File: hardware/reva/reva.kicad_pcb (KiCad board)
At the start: 2 copper layers, 65 x 28 mm, 9 parts, among them U1 ATSAMD21E17D-A, U2 DRV8833PWP, U3 MIC5504-3.3YM5, Y1 Crystal

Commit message: pcb placement
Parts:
- added C1: 10u 16V, Capacitor_SMD:C_0603_1608Metric, F.Cu at (132.0, 96.5)
- added C10: 10u 10V, Capacitor_SMD:C_0603_1608Metric, F.Cu at (149.2, 97.0)
- added C11: 100n, Capacitor_SMD:C_0603_1608Metric, F.Cu at (144.2, 102.0)
- added C12: 10n, Capacitor_SMD:C_0603_1608Metric, F.Cu at (161.0, 87.5)
- added C13: 2u2, Capacitor_SMD:C_0603_1608Metric, F.Cu at (161.0, 84.5)
- added C2: 1n, Capacitor_SMD:C_0603_1608Metric, F.Cu at (130.7, 89.0)
- added C3: 1n, Capacitor_SMD:C_0603_1608Metric, F.Cu at (130.5, 91.0)
- added C4: 10u 10V, Capacitor_SMD:C_0603_1608Metric, F.Cu at (135.0, 98.4)
- added C5: C, Capacitor_SMD:C_0603_1608Metric, F.Cu at (135.0, 101.8)
- added C6: C, Capacitor_SMD:C_0603_1608Metric, F.Cu at (142.0, 102.0)
- added C7: 10n, Capacitor_SMD:C_0603_1608Metric, F.Cu at (177.5, 101.5)
- added C8: 1u 25V, Capacitor_SMD:C_0603_1608Metric, F.Cu at (134.5, 95.0)
- added C9: 100n, Capacitor_SMD:C_0603_1608Metric, F.Cu at (134.8, 91.0)
- added D1: D_Schottky, Diode_SMD:D_SMA, F.Cu at (129.5, 93.8)
- added D2: LED, LED_SMD:LED_0603_1608Metric, F.Cu at (165.8, 102.0)
- added D3: LED, LED_SMD:LED_0603_1608Metric, F.Cu at (162.4, 102.0)
- added D4: LED, LED_SMD:LED_0603_1608Metric, F.Cu at (159.2, 102.0)
- added D5: LED, LED_SMD:LED_0603_1608Metric, F.Cu at (155.7, 102.0)
- added D6: PRTR5V0U2X, Package_TO_SOT_SMD:SOT-143, F.Cu at (129.5, 86.0)
- added D7: D_Schottky, Diode_SMD:D_SMA, F.Cu at (174.8, 90.2)
- added D8: Power, LED_SMD:LED_0603_1608Metric, F.Cu at (125.2, 85.7)
- added FB1: BLM18PG471SZ1D, Inductor_SMD:L_0603_1608Metric, F.Cu at (128.0, 90.0)
- added FB2: BLM18PG471SZ1D, Inductor_SMD:L_0603_1608Metric, F.Cu at (149.2, 100.8)
- added J1: Conn_02x05_Odd_Even, Connector_PinHeader_2.54mm:PinHeader_2x05_P2.54mm_Horizontal, F.Cu at (181.2, 85.0)
- added J2: Conn_01x05, Connector_PinHeader_2.54mm:PinHeader_1x05_P2.54mm_Vertical, F.Cu at (150.4, 79.0)
- added R1: 10k, Resistor_SMD:R_0603_1608Metric, F.Cu at (157.6, 91.8)
- added R10: 330, Resistor_SMD:R_0603_1608Metric, F.Cu at (157.4, 102.0)
- added R11: 27, Resistor_SMD:R_0603_1608Metric, F.Cu at (139.0, 87.0)
- added R12: 27, Resistor_SMD:R_0603_1608Metric, F.Cu at (137.0, 87.0)
- added R13: 330, Resistor_SMD:R_0603_1608Metric, F.Cu at (174.8, 82.4)
- added R14: R, Resistor_SMD:R_0603_1608Metric, F.Cu at (148.5, 84.5)
- added R15: R, Resistor_SMD:R_0603_1608Metric, F.Cu at (148.5, 87.0)
- added R16: 10k, Resistor_SMD:R_0603_1608Metric, F.Cu at (174.8, 100.5)
- added R17: 10k, Resistor_SMD:R_0603_1608Metric, F.Cu at (179.0, 81.8)
- added R18: 10k, Resistor_SMD:R_0603_1608Metric, F.Cu at (149.0, 89.5)
- added R19: 330, Resistor_SMD:R_0603_1608Metric, F.Cu at (125.2, 89.5)
- added R2: 10k, Resistor_SMD:R_0603_1608Metric, F.Cu at (149.8, 93.2)
- added R20: 330, Resistor_SMD:R_0603_1608Metric, F.Cu at (177.0, 96.5)
- added R21: 330, Resistor_SMD:R_0603_1608Metric, F.Cu at (177.0, 93.8)
- added R3: 5k1, Resistor_SMD:R_0603_1608Metric, F.Cu at (135.0, 87.0)
- added R4: 10k, Resistor_SMD:R_0603_1608Metric, F.Cu at (168.0, 92.0)
- added R5: 5k1, Resistor_SMD:R_0603_1608Metric, F.Cu at (141.0, 87.0)
- added R6: 10k, Resistor_SMD:R_0603_1608Metric, F.Cu at (170.8, 82.4)
- added R7: 330, Resistor_SMD:R_0603_1608Metric, F.Cu at (167.6, 102.0)
- added R8: 330, Resistor_SMD:R_0603_1608Metric, F.Cu at (164.2, 102.0)
- added R9: 330, Resistor_SMD:R_0603_1608Metric, F.Cu at (160.9, 102.0)
- added SW1: Mode, Switches_SMD:PTS636_SMT_G, F.Cu at (161.8, 95.2)
- added SW2: Up, Switches_SMD:PTS636_SMT_G, F.Cu at (152.8, 97.4)
- added SW3: Down, Switches_SMD:PTS636_SMT_G, F.Cu at (170.6, 97.6)
- added SW4: Sel, Switches_SMD:PTS636_SMT_G, F.Cu at (173.6, 78.8)
- added SW5: Reset, Switches_SMD:PTS636_SMT_G, F.Cu at (173.6, 86.0)
- moved Y1 25.8 mm to (139.0, 102.0)
- moved U3 24.5 mm to (132.0, 99.5), turned to 270 degrees
- moved U2 14.1 mm to (155.0, 86.0)
- moved U1 3.82 mm to (141.5, 95.0), turned to 90 degrees
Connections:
- U1 pad 1: (no net) -> Net-(C5-Pad1)
- U1 pad 10: Net-(U1-Pad10) -> GND
- U1 pad 13: (no net) -> Net-(R20-Pad1)
- U1 pad 14: (no net) -> Net-(R21-Pad1)
- U1 pad 16: (no net) -> SW_Sel
- U1 pad 2: (no net) -> Net-(C6-Pad1)
- U1 pad 23: (no net) -> /USB_DM
- U1 pad 24: (no net) -> /USB_DP
- U1 pad 26: (no net) -> RESET
- U1 pad 28: Net-(U1-Pad10) -> GND
- U1 pad 29: (no net) -> Net-(C8-Pad1)
- U1 pad 30: (no net) -> +3V3
- U1 pad 31: (no net) -> SWCLK
- U1 pad 32: (no net) -> SWDIO
- U1 pad 9: (no net) -> Net-(C10-Pad1)
- U2 pad 11: (no net) -> Net-(C12-Pad1)
- U2 pad 12: (no net) -> VDC
- U2 pad 13: (no net) -> GND
- U2 pad 14: (no net) -> Net-(C13-Pad2)
- U2 pad 17: Net-(U2-Pad17) -> GND
- U2 pad 2: (no net) -> Net-(J2-Pad1)
- U2 pad 3: (no net) -> Net-(R14-Pad1)
- U2 pad 4: (no net) -> Net-(J2-Pad2)
- U2 pad 5: (no net) -> Net-(J2-Pad5)
- U2 pad 6: (no net) -> Net-(R15-Pad1)
- U2 pad 7: (no net) -> Net-(J2-Pad4)
- U2 pad 8: (no net) -> FAULT
- U3 pad 1: (no net) -> VDC
- U3 pad 2: (no net) -> GND
- U3 pad 3: (no net) -> VDC
- U3 pad 5: (no net) -> +3V3
- USB1 pad 1: (no net) -> GND
- USB1 pad 10: (no net) -> Net-(R3-Pad1)
- USB1 pad 11: (no net) -> VCC
- USB1 pad 12: (no net) -> GND
- USB1 pad 13: Net-(USB1-Pad13) -> GND
- USB1 pad 2: (no net) -> VCC
- USB1 pad 4: (no net) -> Net-(R5-Pad1)
- USB1 pad 5: (no net) -> Net-(R11-Pad2)
- USB1 pad 6: (no net) -> Net-(R12-Pad2)
- USB1 pad 7: (no net) -> Net-(R11-Pad2)
- USB1 pad 8: (no net) -> Net-(R12-Pad2)
- Y1 pad 1: (no net) -> Net-(C5-Pad1)
- Y1 pad 2: (no net) -> Net-(C6-Pad1)

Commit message: connections
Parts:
- added R22: 10k, Resistor_SMD:R_0603_1608Metric, F.Cu at (161.7, 89.3)
- moved R18 14.5 mm to (161.7, 82.5), turned to 180 degrees
- moved R14 13.5 mm to (161.7, 87.5), turned to 0 degrees
- moved R15 13.4 mm to (161.7, 85.0), turned to 0 degrees
- moved C12 12.2 mm to (149.2, 84.5), turned to 270 degrees
- moved C13 12.2 mm to (149.2, 87.5), turned to 270 degrees
- moved C8 0.50 mm to (135.0, 95.0)
- moved C9 0.25 mm to (135.0, 91.0)
- moved C2 0.22 mm to (130.5, 89.0)
- moved U2 0.20 mm to (155.2, 86.0), turned to 180 degrees
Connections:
- D2 pad 1: (no net) -> Net-(D2-Pad1)
- D3 pad 1: (no net) -> Net-(D3-Pad1)
- D4 pad 1: (no net) -> Net-(D4-Pad1)
- D5 pad 1: (no net) -> Net-(D5-Pad1)
- U1 pad 12: (no net) -> SW_Mode
- U1 pad 15: (no net) -> SW_Down
- U1 pad 17: (no net) -> SW_Up
- U1 pad 18: (no net) -> nSleep
- U1 pad 19: (no net) -> AIN1
- U1 pad 20: (no net) -> AIN2
- U1 pad 21: (no net) -> BIN1
- U1 pad 22: (no net) -> BIN2
- U1 pad 25: (no net) -> FAULT
- U1 pad 3: (no net) -> Net-(D2-Pad1)
- U1 pad 4: (no net) -> Net-(D3-Pad1)
- U1 pad 5: (no net) -> Net-(D4-Pad1)
- U1 pad 6: (no net) -> Net-(D5-Pad1)
- U2 pad 1: (no net) -> nSleep
- U2 pad 10: (no net) -> BIN2
- U2 pad 15: (no net) -> AIN2
- U2 pad 16: (no net) -> AIN1
- U2 pad 9: (no net) -> BIN1

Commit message: layout final
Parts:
- H1, H2, H3, H4: footprint MountingHole:MountingHole_3.2mm_M3_DIN965 -> MountingHole:MountingHole_3.2mm_M3_DIN965_Pad
- moved R13 16.0 mm to (177.5, 98.2)
- moved R18 13.7 mm to (148.3, 85.3), turned to 0 degrees
- moved R15 12.3 mm to (149.8, 81.7), turned to 180 degrees
- moved R2 10.1 mm to (159.7, 91.1), turned to 270 degrees
- moved C13 8.57 mm to (156.6, 91.9), turned to 0 degrees
- moved C12 7.79 mm to (153.4, 91.0), turned to 0 degrees
- moved R14 5.92 mm to (160.1, 81.8)
- moved R6 5.40 mm to (176.2, 82.3), turned to 90 degrees
- moved R22 5.14 mm to (160.1, 84.4)
- moved R1 4.01 mm to (161.6, 91.1)
- moved R16 1.20 mm to (175.8, 99.8), turned to 0 degrees
- moved R17 1.12 mm to (178.0, 82.3), turned to 90 degrees
- moved U2 0.38 mm to (154.8, 85.8), turned to 270 degrees
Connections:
- net /USB_DM renamed USB_DM
- net /USB_DP renamed USB_DP
- D6 pad 2: (no net) -> /_DP
- D6 pad 3: (no net) -> /_DM
- H1 pad 1: (no net) -> GND
- H2 pad 1: (no net) -> GND
- H3 pad 1: (no net) -> GND
- H4 pad 1: (no net) -> GND
- J2 pad 1: Net-(J2-Pad1) -> /B1
- J2 pad 2: Net-(J2-Pad2) -> /B2
- J2 pad 4: Net-(J2-Pad4) -> /A2
- J2 pad 5: Net-(J2-Pad5) -> /A1
- R11 pad 2: Net-(R11-Pad2) -> /_DM
- R12 pad 2: Net-(R12-Pad2) -> /_DP
- U1 pad 21: BIN1 -> BIN2
- U1 pad 22: BIN2 -> BIN1
- U2 pad 2: Net-(J2-Pad1) -> /A1
- U2 pad 4: Net-(J2-Pad2) -> /A2
- U2 pad 5: Net-(J2-Pad5) -> /B2
- U2 pad 7: Net-(J2-Pad4) -> /B1
- USB1 pad 5: Net-(R11-Pad2) -> /_DM
- USB1 pad 6: Net-(R12-Pad2) -> /_DP
- USB1 pad 7: Net-(R11-Pad2) -> /_DM
- USB1 pad 8: Net-(R12-Pad2) -> /_DP
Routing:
- net +3V3: track 0.00 -> 135.7 mm, vias 0 -> 10
- net GND: track 0.00 -> 120.0 mm, vias 0 -> 71
- net VDC: track 0.00 -> 77.4 mm, vias 0 -> 3
- net SWCLK: track 0.00 -> 71.2 mm, vias 0 -> 1
- net SW_Sel: track 0.00 -> 65.0 mm, vias 0 -> 2
- net SWDIO: track 0.00 -> 59.1 mm, vias 0 -> 1
- net RESET: track 0.00 -> 56.9 mm, vias 0 -> 2
- net Net-(R21-Pad1): track 0.00 -> 32.7 mm
- net Net-(R20-Pad1): track 0.00 -> 31.9 mm
- net Net-(D2-Pad1): track 0.00 -> 31.0 mm, vias 0 -> 2
- net SW_Up: track 0.00 -> 29.2 mm, vias 0 -> 2
- net FAULT: track 0.00 -> 26.2 mm, vias 0 -> 2
- net Net-(D3-Pad1): track 0.00 -> 26.1 mm, vias 0 -> 2
- net nSleep: track 0.00 -> 23.7 mm, vias 0 -> 2
- net Net-(D4-Pad1): track 0.00 -> 21.1 mm, vias 0 -> 2
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- added copper zone on B.Cu, net GND
- added copper zone on F.Cu, net GND
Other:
- net class Default: trace_width 0.25 -> 0.15; via_dia 0.8 -> 0.6; via_drill 0.4 -> 0.3
- rule trace_min: 0.2 -> 0.15
- rule via_min_size: 0.4 -> 0.6
- board text added: "Mode"
- board text added: "Reset"
- board text added: "RevA 05/2021 ML"
- board text added: "Sel"

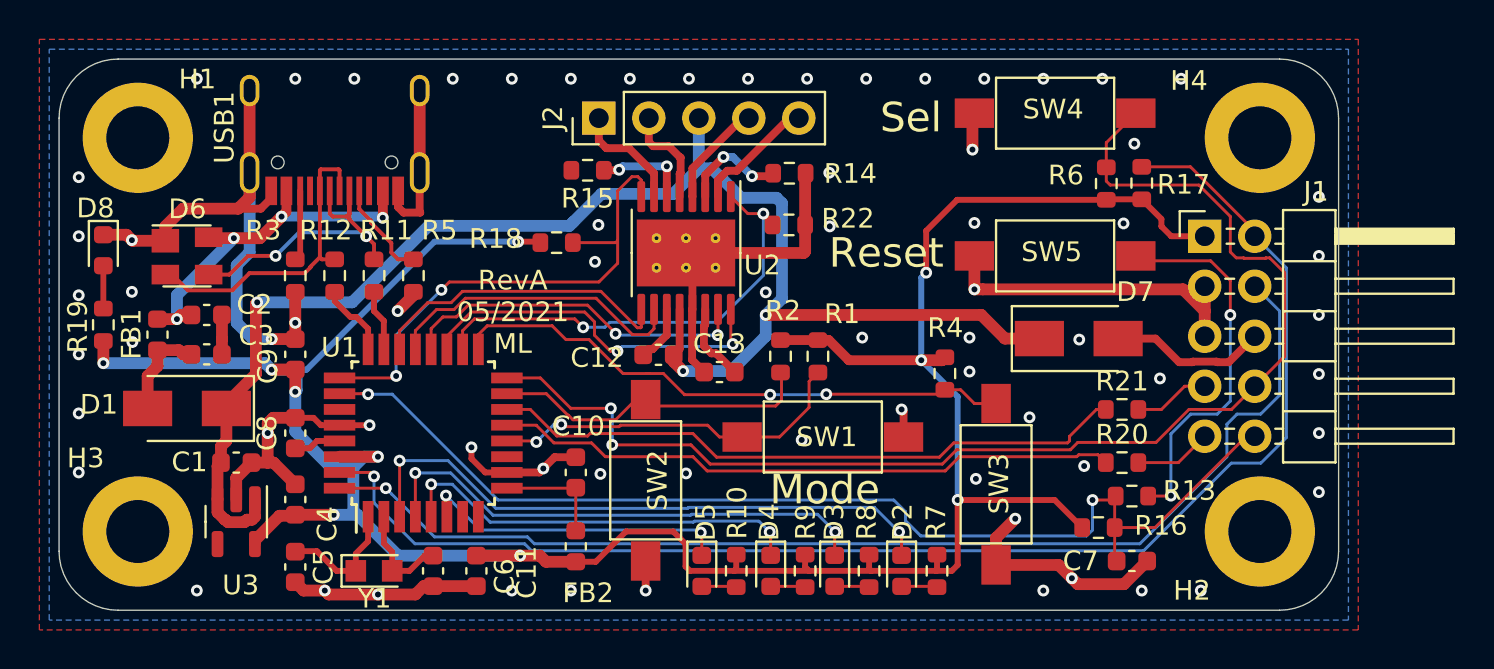
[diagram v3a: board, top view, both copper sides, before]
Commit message: added con for Sel, added gerber
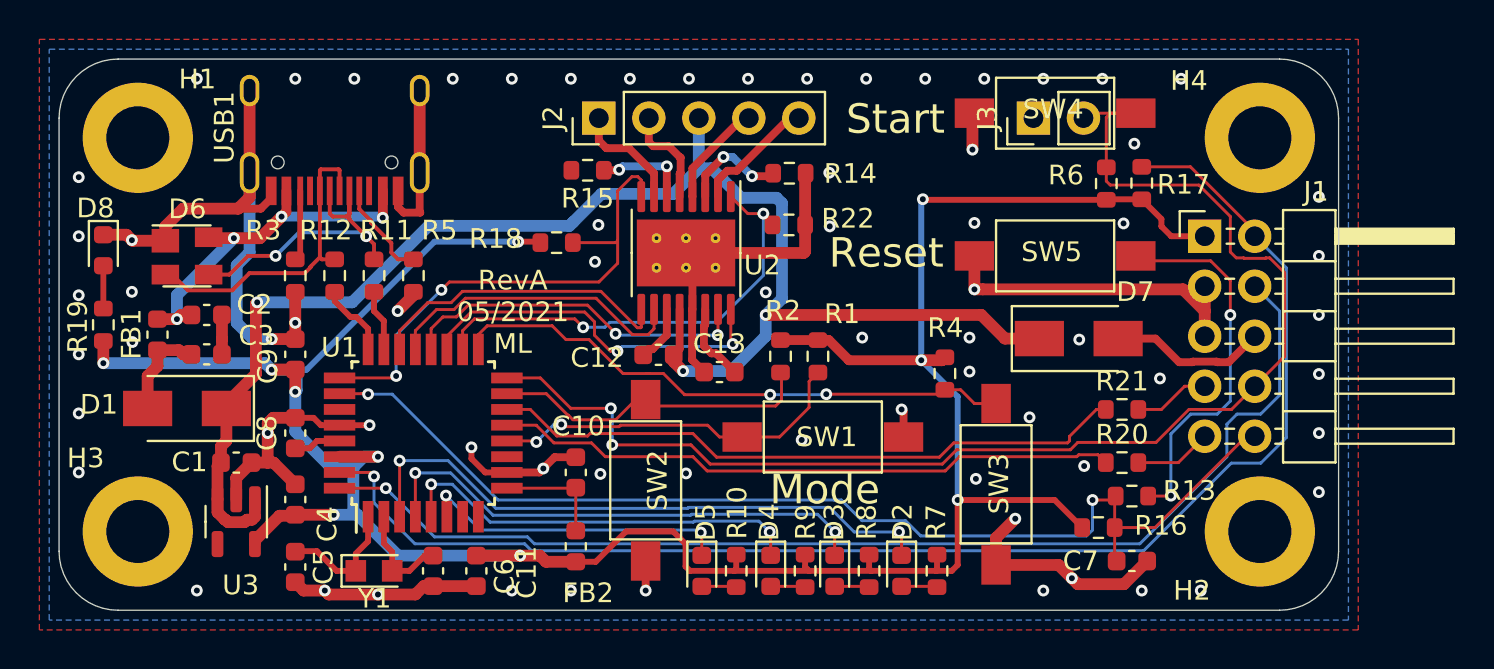
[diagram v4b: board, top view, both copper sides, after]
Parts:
- added J3: Conn_01x02, Connector_PinHeader_2.54mm:PinHeader_1x02_P2.54mm_Vertical, F.Cu at (172.5, 79.0)
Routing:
- net SW_Sel: track 65.0 -> 68.5 mm
- net +3V3: track 135.7 -> 136.8 mm
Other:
- board text added: "Start"
- board text removed: "Sel"
